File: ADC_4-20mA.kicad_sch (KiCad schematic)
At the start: 28 parts, among them J20 1862424, J21 1862424, J22 1862424, J23 1862424, U5 REF5050IDGK, U6 ADS1256IDBT, Y2 Crystal

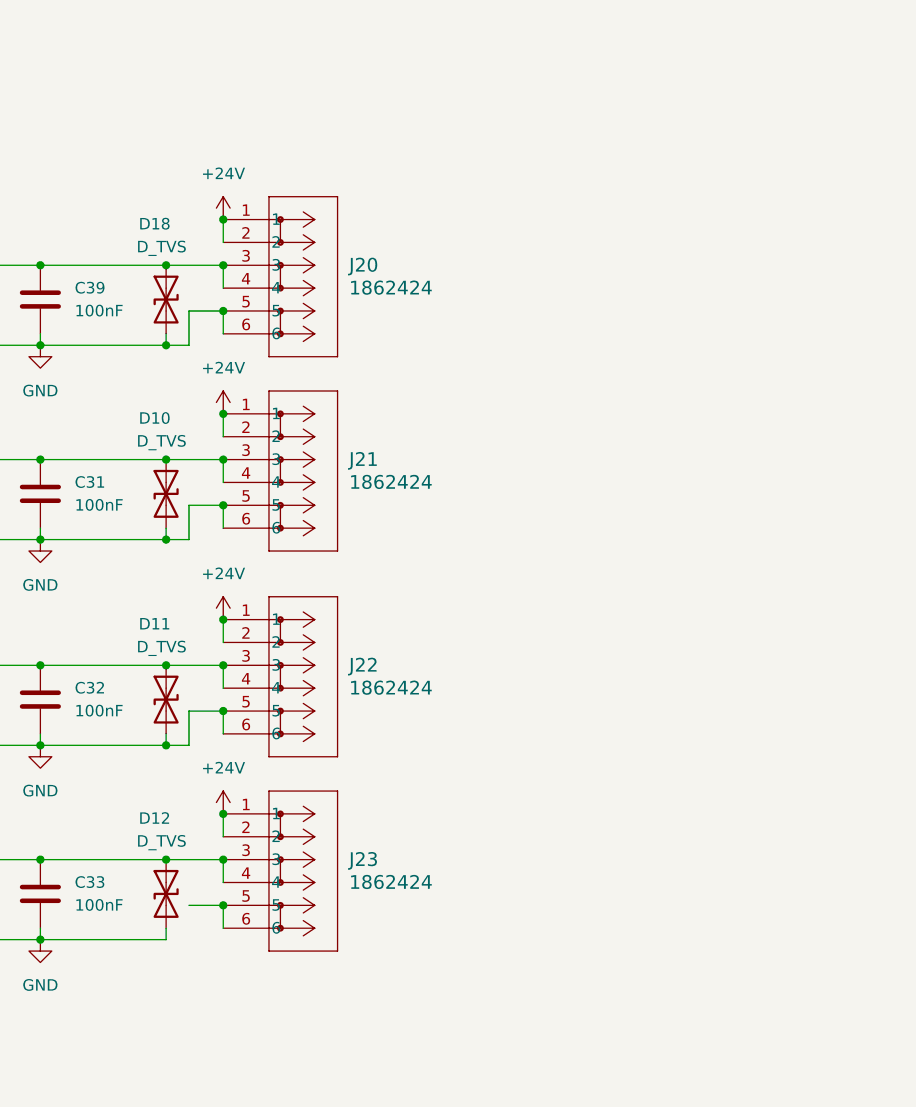
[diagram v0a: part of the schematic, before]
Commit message: Updated schematic and PCB
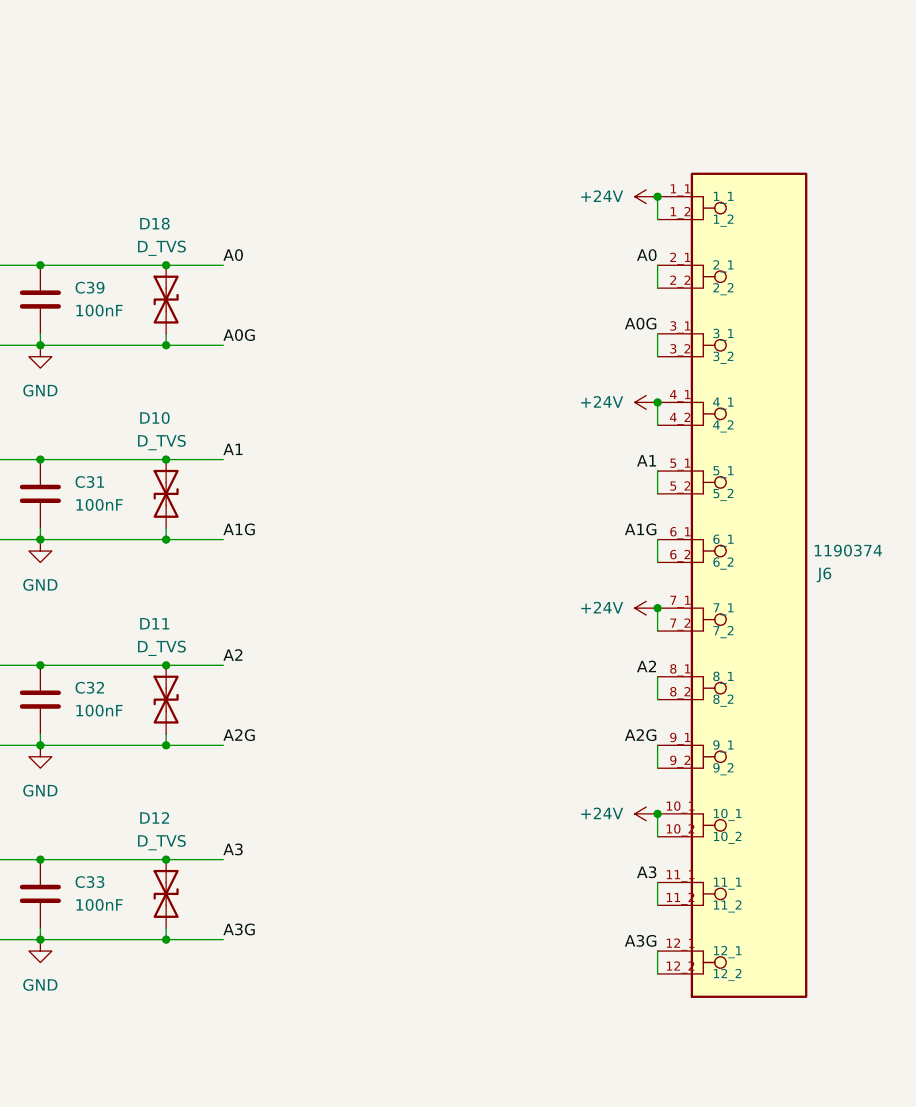
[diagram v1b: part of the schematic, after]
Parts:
- removed J20, J21, J22, J23: 1862424, CONN_1862424, symbol 2026-03-28_19-29-49:1862424
- added J6: 1190374, LPTA 2,512-5,0 - PCB terminal block1:PHOENIX_1190374, symbol 1190374:1190374
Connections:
- net +24V: now also J6.10_1, J6.10_2, J6.1_1, J6.1_2, J6.4_1, J6.4_2, J6.7_1, J6.7_2
- net GND: now also J6.12_1, J6.12_2, J6.3_1, J6.3_2, J6.6_1, J6.6_2, J6.9_1, J6.9_2
- net AIN0 renamed A0
- net A0: now also J6.2_1, J6.2_2
- net AIN1 renamed A1
- net A1: now also J6.5_1, J6.5_2
- net AIN2 renamed A2
- net A2: now also J6.8_1, J6.8_2
- net AIN3 renamed A3
- net A3: now also J6.11_1, J6.11_2
